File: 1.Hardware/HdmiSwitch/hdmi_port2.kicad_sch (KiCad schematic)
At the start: 16 parts

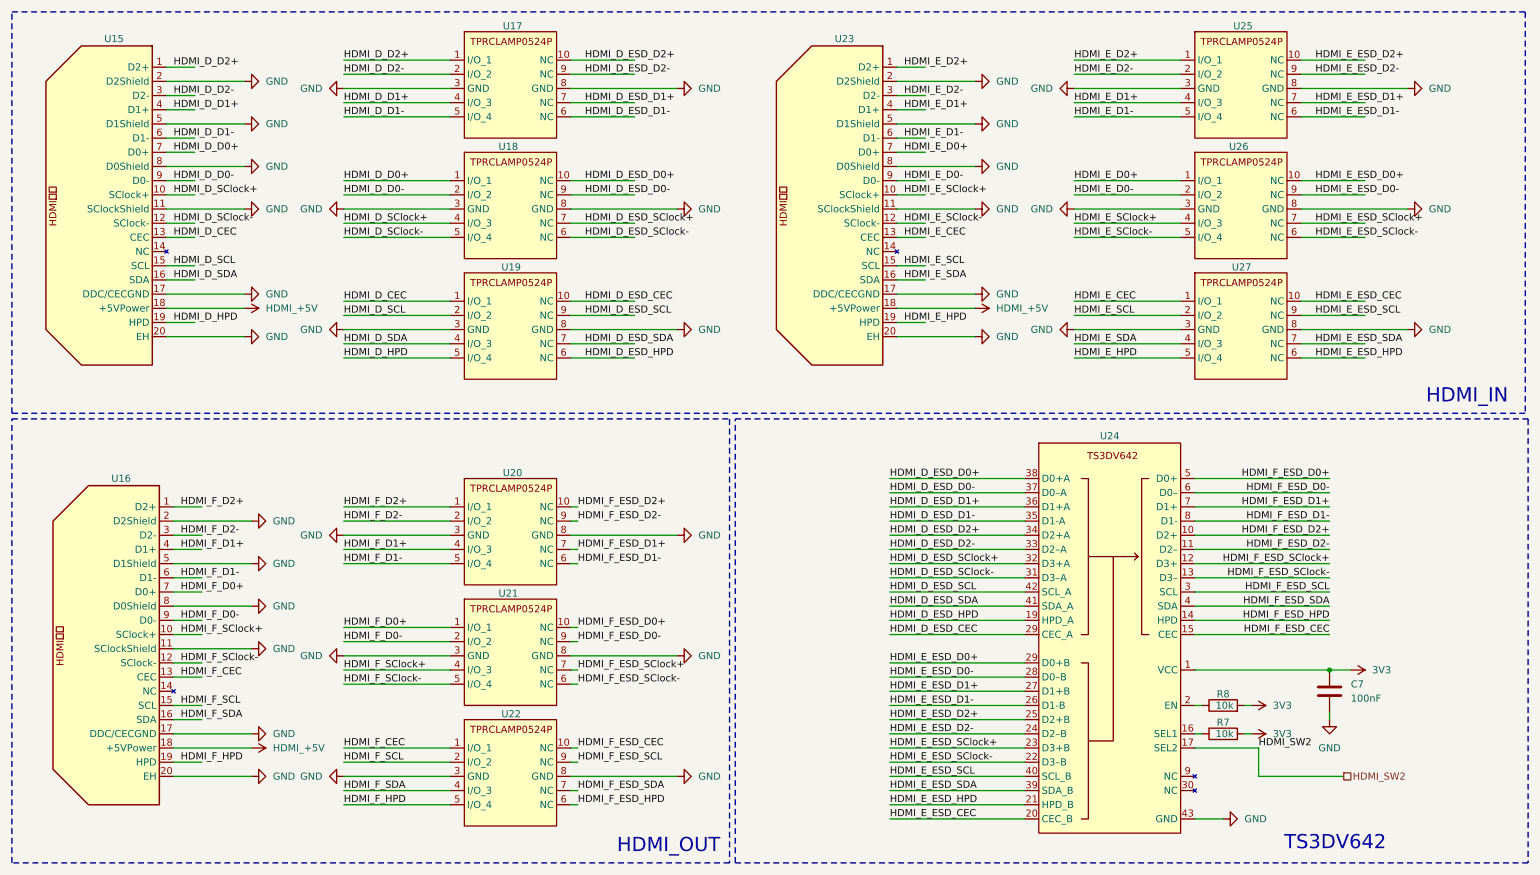
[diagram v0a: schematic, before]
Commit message: 为HDMISwitch模块添加了封装模型
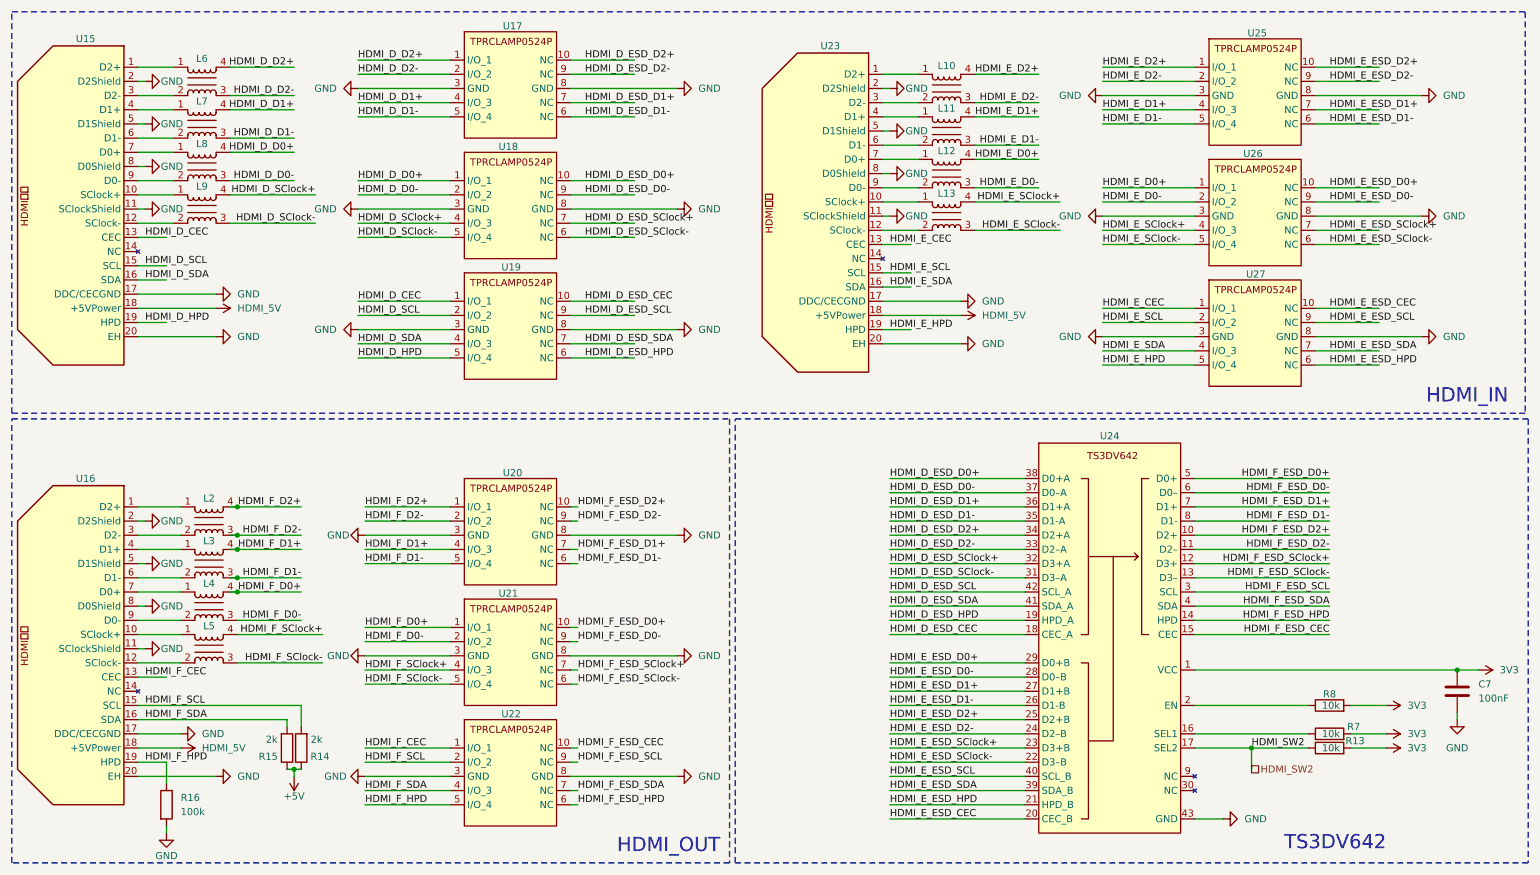
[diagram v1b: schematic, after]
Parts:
- added L10, L11, L12, L13, L2, L3, L4, L5, L6, L7, L8, L9: ~, HdmiSwitch:ACM2012-900-2P-T002, symbol HdmiSwitch:ACM2012-900-2P-T002
- added R13: 10k, Resistor_SMD:R_0402_1005Metric, symbol Device:R
- added R14: 2k, Capacitor_SMD:C_0402_1005Metric, symbol Device:R
- added R15: 2k, Resistor_SMD:R_0402_1005Metric, symbol Device:R
- added R16: 100k, Resistor_SMD:R_0402_1005Metric, symbol Device:R
- C7: footprint (none) -> Capacitor_SMD:C_0402_1005Metric
- R7, R8: footprint (none) -> Resistor_SMD:R_0402_1005Metric
- U15, U16, U23: footprint (none) -> HdmiSwitch:HDMI侧插
- U17, U18, U19, U20, U21, U22, U25, U26, U27: footprint (none) -> HdmiSwitch:TPRCLAMP0524P
- U24: footprint (none) -> HdmiSwitch:TS3DV642
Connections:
- net 3V3: now also R13.2
- net GND: now also R16.2
- net HDMI_D_D0+: now also L8.4; no longer U15.7 (D0+)
- net HDMI_D_D0-: now also L8.3; no longer U15.9 (D0-)
- net HDMI_D_D1+: now also L7.4; no longer U15.4 (D1+)
- net HDMI_D_D1-: now also L7.3; no longer U15.6 (D1-)
- net HDMI_D_D2+: now also L6.4; no longer U15.1 (D2+)
- net HDMI_D_D2-: now also L6.3; no longer U15.3 (D2-)
- net HDMI_D_ESD_CEC: now also U24.18 (CEC_A); no longer U24.29 (D0+B)
- net HDMI_D_SClock+: now also L9.4; no longer U15.10 (SClock+)
- net HDMI_D_SClock-: now also L9.3; no longer U15.12 (SClock-)
- net HDMI_E_D0+: now also L12.4; no longer U23.7 (D0+)
- net HDMI_E_D0-: now also L12.3; no longer U23.9 (D0-)
- net HDMI_E_D1+: now also L11.4; no longer U23.4 (D1+)
- net HDMI_E_D1-: now also L11.3; no longer U23.6 (D1-)
- net HDMI_E_D2+: now also L10.4; no longer U23.1 (D2+)
- net HDMI_E_D2-: now also L10.3; no longer U23.3 (D2-)
- net HDMI_E_SClock+: now also L13.4; no longer U23.10 (SClock+)
- net HDMI_E_SClock-: now also L13.3; no longer U23.12 (SClock-)
- net HDMI_F_D0+: now also L4.4; no longer U16.7 (D0+)
- net HDMI_F_D0-: now also L4.3; no longer U16.9 (D0-)
- net HDMI_F_D1+: now also L3.4; no longer U16.4 (D1+)
- net HDMI_F_D1-: now also L3.3; no longer U16.6 (D1-)
- net HDMI_F_D2+: now also L2.4; no longer U16.1 (D2+)
- net HDMI_F_D2-: now also L2.3; no longer U16.3 (D2-)
- net HDMI_F_HPD: now also R16.1
- net HDMI_F_SCL: now also R14.2
- net HDMI_F_SClock+: now also L5.4; no longer U16.10 (SClock+)
- net HDMI_F_SClock-: now also L5.3; no longer U16.12 (SClock-)
- net HDMI_F_SDA: now also R15.2
- net HDMI_SW2: now also R13.1
- net HDMI_+5V renamed HDMI_5V
- new net: L3.1, U16.4 (D1+)
- new net: L3.2, U16.6 (D1-)
- new net: L5.1, U16.10 (SClock+)
- new net: L5.2, U16.12 (SClock-)
- new net: L13.1, U23.10 (SClock+)
- new net: L13.2, U23.12 (SClock-)
- new net: L12.1, U23.7 (D0+)
- new net: L12.2, U23.9 (D0-)
- new net: L9.1, U15.10 (SClock+)
- new net: L9.2, U15.12 (SClock-)
- new net: L8.1, U15.7 (D0+)
- new net: L8.2, U15.9 (D0-)
- new net: L11.1, U23.4 (D1+)
- new net: L11.2, U23.6 (D1-)
- new net: L7.1, U15.4 (D1+)
- new net: L7.2, U15.6 (D1-)
- new net: L4.1, U16.7 (D0+)
- new net: L4.2, U16.9 (D0-)
- new net: L10.1, U23.1 (D2+)
- new net: L10.2, U23.3 (D2-)
- new net: L2.1, U16.1 (D2+)
- new net: L2.2, U16.3 (D2-)
- new net: L6.1, U15.1 (D2+)
- new net: L6.2, U15.3 (D2-)
- new net +5V: R14.1, R15.1
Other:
- moved on the sheet: C7, R7, R8, U15, U16
